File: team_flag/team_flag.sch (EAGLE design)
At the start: 9 parts, among them Q1 MOSFET-LOGIC-NCHANNELSMD, Q2 MOSFET-LOGIC-NCHANNELSMD

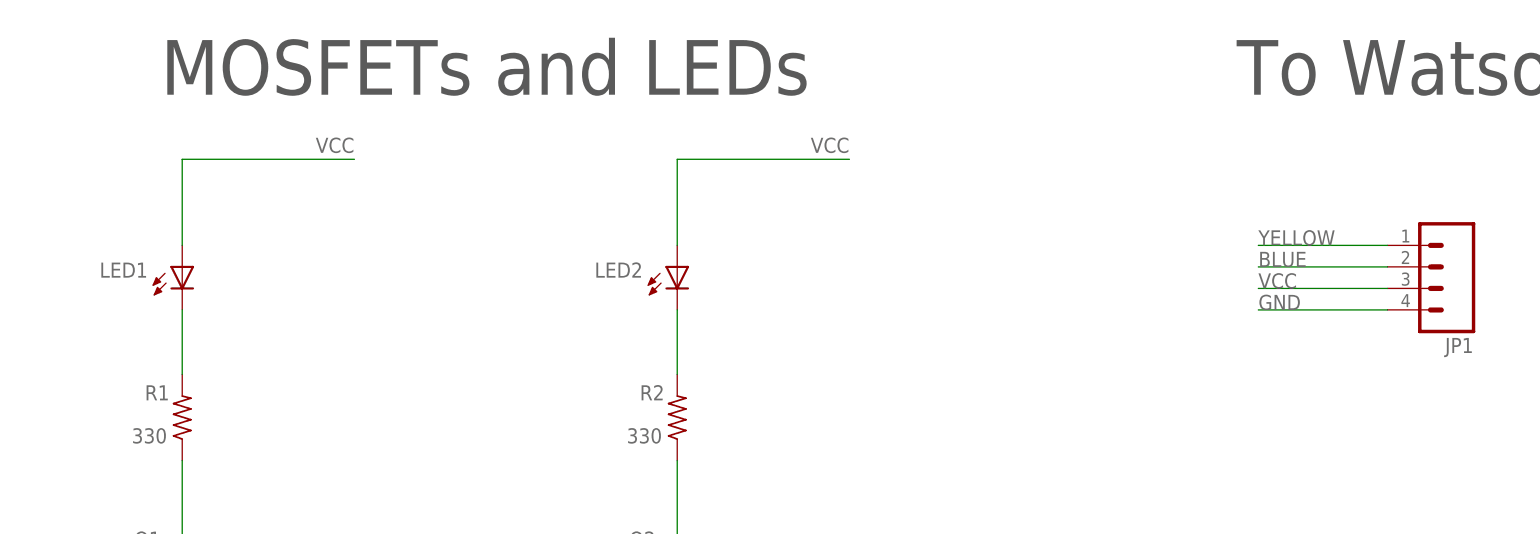
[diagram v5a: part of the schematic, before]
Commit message: Team flag silk changes as per Casey and Aravind's requests
changed resistor values to 200 ohm, new LED footprint to show which
side is anode/cathode, maybe other silkscreen changes?

Basically, this is Sumita's Team Flag, but with my new LED footprint
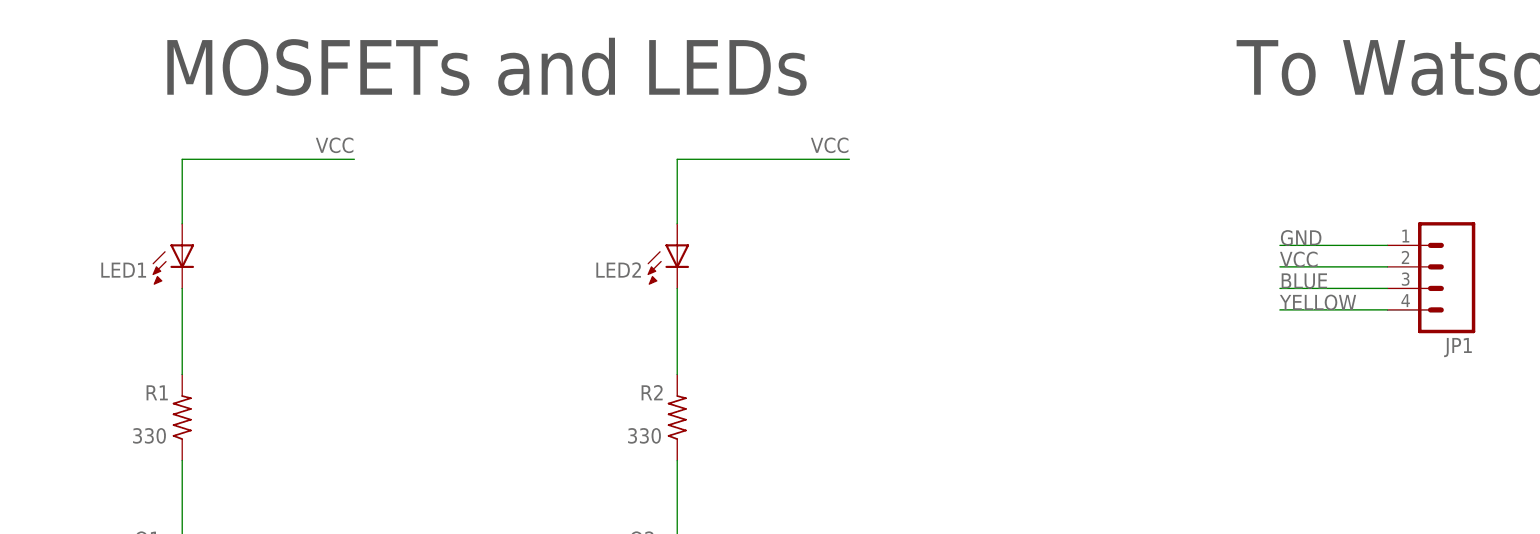
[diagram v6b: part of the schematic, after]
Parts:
- LED1, LED2: device led:LED5MM -> pie:LEDLED5MM-NOFLAT
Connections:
- net BLUE: now also JP1.3; no longer JP1.2
- net GND: now also JP1.1; no longer JP1.4
- net VCC: now also JP1.2; no longer JP1.3
- net YELLOW: now also JP1.4; no longer JP1.1
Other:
- moved on the sheet: LED1, LED2
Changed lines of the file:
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@@
 <layer number="97" name="Info" color="7" fill="1" visible="yes" active="yes"/>
 <layer number="98" name="Guide" color="6" fill="1" visible="yes" active="yes"/>
+<layer number="99" name="SpiceOrder" color="5" fill="1" visible="yes" active="yes"/>
 <layer number="100" name="Muster" color="7" fill="1" visible="no" active="no"/>
 <layer number="101" name="Patch_Top" color="12" fill="4" visible="yes" active="yes"/>
@@
 </classes>
 <parts>
-<part name="LED1" library="led" deviceset="LED" device="5MM"/>
-<part name="LED2" library="led" deviceset="LED" device="5MM"/>
+<part name="LED1" library="pie" deviceset="LED" device="LED5MM-NOFLAT"/>
+<part name="LED2" library="pie" deviceset="LED" device="LED5MM-NOFLAT"/>
 <part name="R1" library="rcl" deviceset="R-US_" device="R0603" value="330"/>
 <part name="R2" library="rcl" deviceset="R-US_" device="R0603" value="330"/>
@@
 </segment>
 <segment>
-<pinref part="JP1" gate="G$1" pin="1"/>
-<wire x1="187.96" y1="86.36" x2="172.72" y2="86.36" width="0.1524" layer="91"/>
-<label x="172.72" y="86.36" size="1.778" layer="95"/>
+<pinref part="JP1" gate="G$1" pin="4"/>
+<wire x1="187.96" y1="78.74" x2="175.26" y2="78.74" width="0.1524" layer="91"/>
+<label x="175.26" y="78.74" size="1.778" layer="95"/>
 </segment>
 </net>
@@
 <label x="124.46" y="99.06" size="1.778" layer="95" rot="R180"/>
 <pinref part="LED2" gate="G$1" pin="A"/>
-<wire x1="104.14" y1="96.52" x2="104.14" y2="86.36" width="0.1524" layer="91"/>
+<wire x1="104.14" y1="96.52" x2="104.14" y2="88.9" width="0.1524" layer="91"/>
 </segment>
 <segment>
@@
 <label x="66.04" y="99.06" size="1.778" layer="95" rot="R180"/>
 <pinref part="LED1" gate="G$1" pin="A"/>
-<wire x1="45.72" y1="96.52" x2="45.72" y2="86.36" width="0.1524" layer="91"/>
-</segment>
-<segment>
-<pinref part="JP1" gate="G$1" pin="3"/>
-<wire x1="187.96" y1="81.28" x2="172.72" y2="81.28" width="0.1524" layer="91"/>
-<label x="172.72" y="81.28" size="1.778" layer="95"/>
+<wire x1="45.72" y1="96.52" x2="45.72" y2="88.9" width="0.1524" layer="91"/>
+</segment>
+<segment>
+<pinref part="JP1" gate="G$1" pin="2"/>
+<wire x1="187.96" y1="83.82" x2="175.26" y2="83.82" width="0.1524" layer="91"/>
+<label x="175.26" y="83.82" size="1.778" layer="95"/>
 </segment>
 </net>
@@
 </segment>
 <segment>
-<pinref part="JP1" gate="G$1" pin="4"/>
-<wire x1="187.96" y1="78.74" x2="172.72" y2="78.74" width="0.1524" layer="91"/>
-<label x="172.72" y="78.74" size="1.778" layer="95"/>
+<pinref part="JP1" gate="G$1" pin="1"/>
+<wire x1="187.96" y1="86.36" x2="175.26" y2="86.36" width="0.1524" layer="91"/>
+<label x="175.26" y="86.36" size="1.778" layer="95"/>
 </segment>
 </net>
@@
 </segment>
 <segment>
-<pinref part="JP1" gate="G$1" pin="2"/>
-<wire x1="187.96" y1="83.82" x2="172.72" y2="83.82" width="0.1524" layer="91"/>
-<label x="172.72" y="83.82" size="1.778" layer="95"/>
+<pinref part="JP1" gate="G$1" pin="3"/>
+<wire x1="187.96" y1="81.28" x2="175.26" y2="81.28" width="0.1524" layer="91"/>
+<label x="175.26" y="81.28" size="1.778" layer="95"/>
 </segment>
 </net>
@@
 <pinref part="R1" gate="G$1" pin="2"/>
 <pinref part="LED1" gate="G$1" pin="C"/>
-<wire x1="45.72" y1="71.12" x2="45.72" y2="78.74" width="0.1524" layer="91"/>
+<wire x1="45.72" y1="71.12" x2="45.72" y2="81.28" width="0.1524" layer="91"/>
 </segment>
 </net>
@@
 <pinref part="LED2" gate="G$1" pin="C"/>
 <pinref part="R2" gate="G$1" pin="2"/>
-<wire x1="104.14" y1="78.74" x2="104.14" y2="71.12" width="0.1524" layer="91"/>
-</segment>
-</net>
+<wire x1="104.14" y1="81.28" x2="104.14" y2="71.12" width="0.1524" layer="91"/>
+</segment>
+</net>

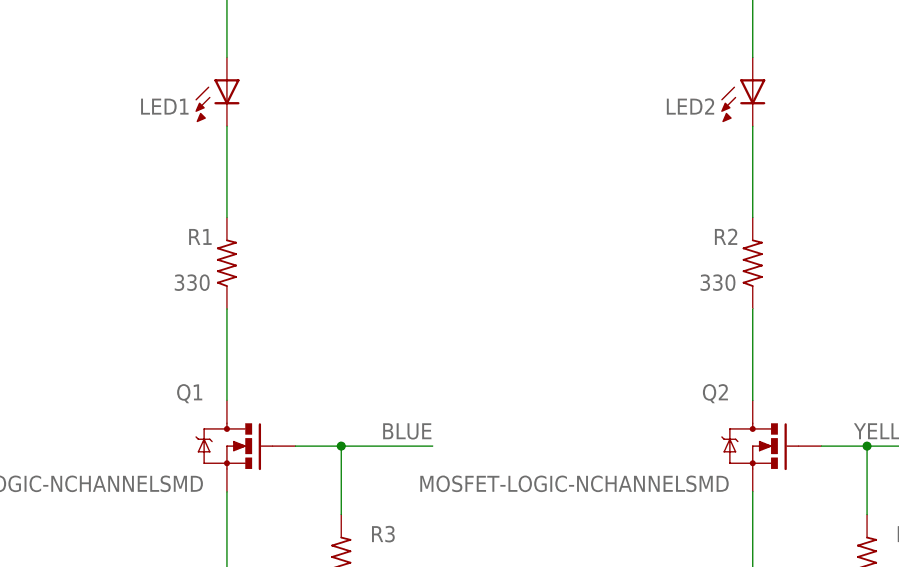
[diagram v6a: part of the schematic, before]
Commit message: set resistor values (on Team flag) to 200 ohms
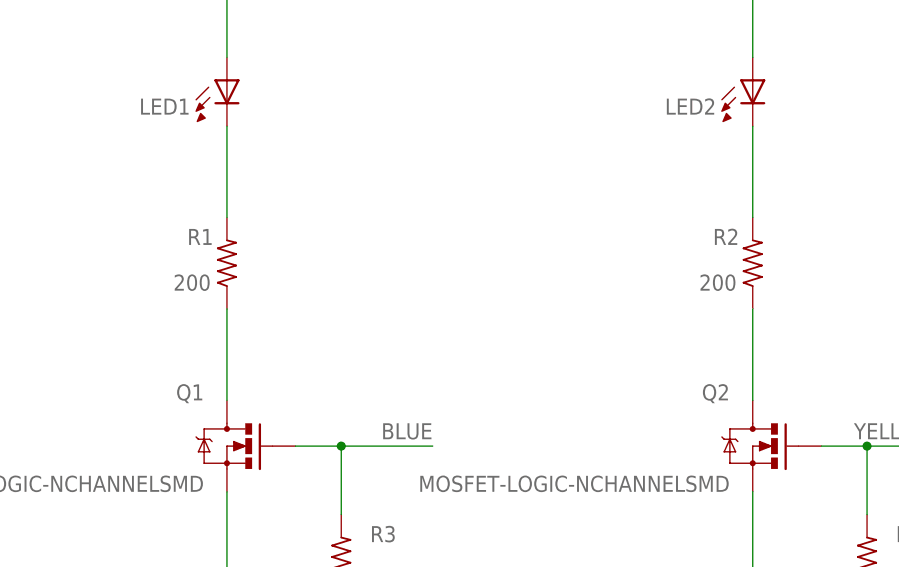
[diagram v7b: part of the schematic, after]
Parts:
- R1, R2: value 330 -> 200
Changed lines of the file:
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@@
 <part name="LED1" library="pie" deviceset="LED" device="LED5MM-NOFLAT"/>
 <part name="LED2" library="pie" deviceset="LED" device="LED5MM-NOFLAT"/>
-<part name="R1" library="rcl" deviceset="R-US_" device="R0603" value="330"/>
-<part name="R2" library="rcl" deviceset="R-US_" device="R0603" value="330"/>
+<part name="R1" library="rcl" deviceset="R-US_" device="R0603" value="200"/>
+<part name="R2" library="rcl" deviceset="R-US_" device="R0603" value="200"/>
 <part name="Q1" library="pie" deviceset="MOSFET-LOGIC-NCHANNEL" device="SMD"/>
 <part name="Q2" library="pie" deviceset="MOSFET-LOGIC-NCHANNEL" device="SMD"/>
